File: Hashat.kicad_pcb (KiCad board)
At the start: 2 copper layers, 65 x 56.5 mm, 5 parts, among them J1 Raspberry_Pi_2_3

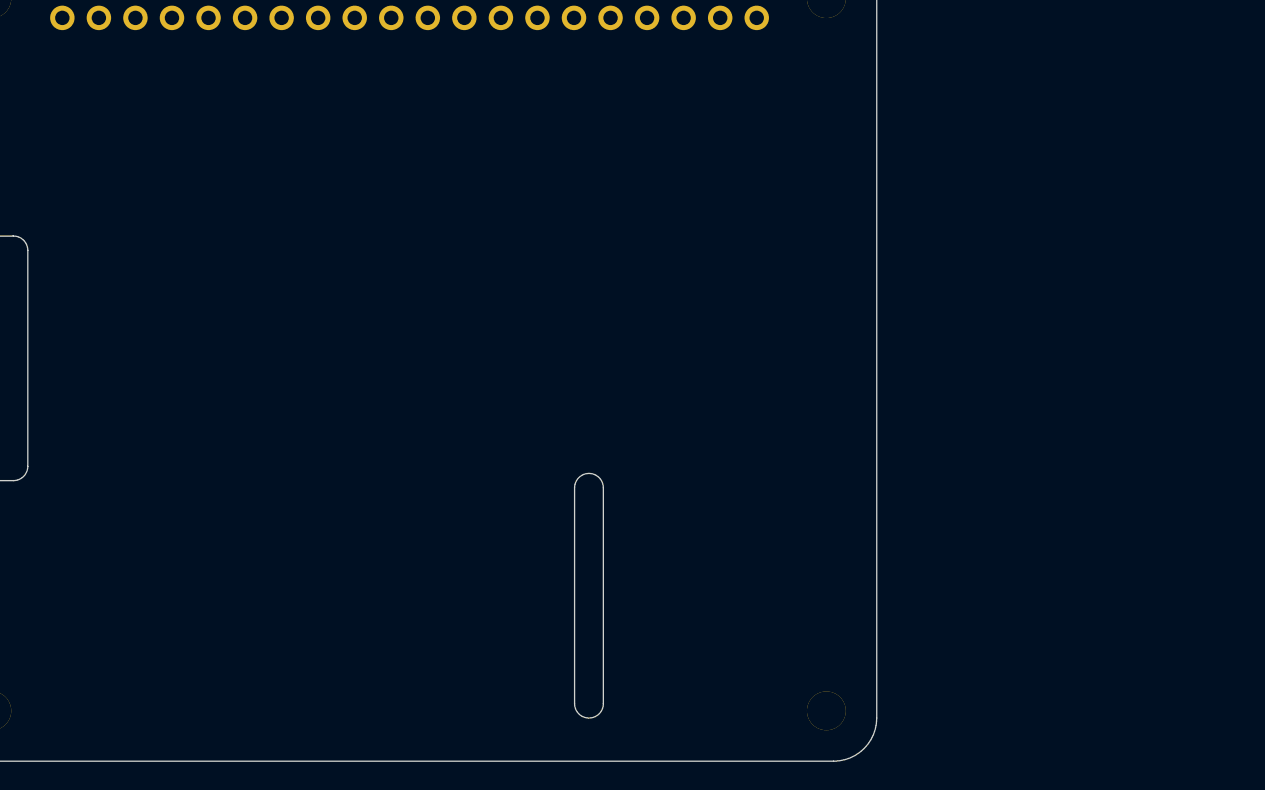
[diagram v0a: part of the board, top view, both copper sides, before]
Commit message: moved over a lot of schematic from the bitaxe
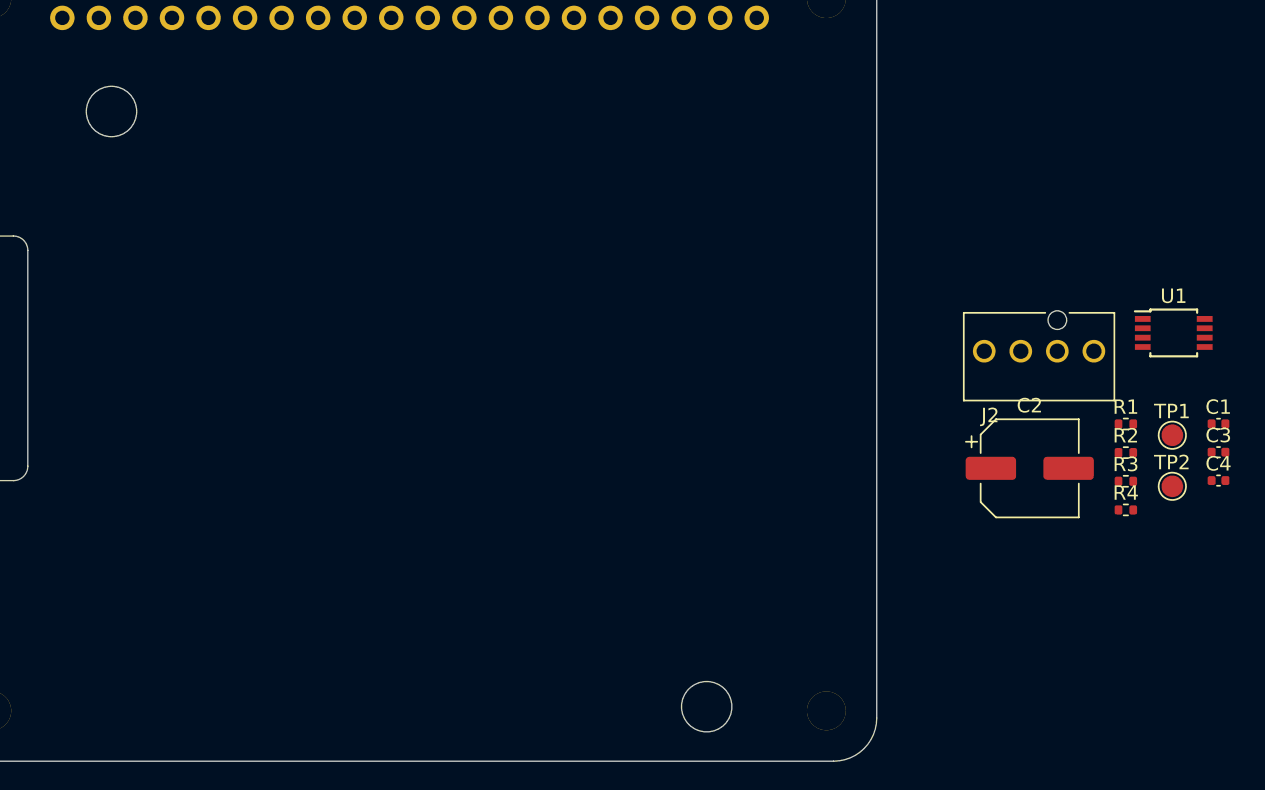
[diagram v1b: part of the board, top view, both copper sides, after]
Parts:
- added C1: 470pF, Capacitor_SMD:C_0402_1005Metric, F.Cu at (165.8, 88.6)
- added C2: 220uF, Capacitor_SMD:CP_Elec_6.3x7.7, F.Cu at (152.6, 91.6)
- added C3: 311-3342-1-ND, Capacitor_SMD:C_0402_1005Metric, F.Cu at (165.8, 90.5)
- added C4: 311-3342-1-ND, Capacitor_SMD:C_0402_1005Metric, F.Cu at (165.8, 92.5)
- added H5: MountingHole, MountingHole:MountingHole_3.5mm, F.Cu at (130.1, 108.2)
- added H6: MountingHole, MountingHole:MountingHole_3.5mm, F.Cu at (88.8, 66.8)
- added J2: Conn_01x04, bitaxe:470531000, F.Cu at (149.5, 83.5)
- added R1: 100, Resistor_SMD:R_0402_1005Metric, F.Cu at (159.3, 88.6)
- added R2: 100, Resistor_SMD:R_0402_1005Metric, F.Cu at (159.3, 90.6)
- added R3: 10k, Resistor_SMD:R_0402_1005Metric, F.Cu at (159.3, 92.5)
- added R4: 10k, Resistor_SMD:R_0402_1005Metric, F.Cu at (159.3, 94.5)
- added TP1: TestPoint, TestPoint:TestPoint_Pad_D1.5mm, F.Cu at (162.5, 89.3)
- added TP2: TestPoint, TestPoint:TestPoint_Pad_D1.5mm, F.Cu at (162.5, 92.9)
- added U1: EMC2101, Package_SO:TSSOP-8_3x3mm_P0.65mm, F.Cu at (162.6, 82.2)
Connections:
- J1 pad 1: Net-(J1-Pad1) -> unconnected-(J1-3V3-Pad1)
- J1 pad 10: Net-(J1-Pad10) -> unconnected-(J1-GPIO15/RXD-Pad10)
- J1 pad 11: Net-(J1-Pad11) -> unconnected-(J1-GPIO17-Pad11)
- J1 pad 12: Net-(J1-Pad12) -> unconnected-(J1-GPIO18/PWM0-Pad12)
- J1 pad 13: Net-(J1-Pad13) -> unconnected-(J1-GPIO27-Pad13)
- J1 pad 14: Net-(J1-Pad14) -> unconnected-(J1-GND-Pad14)
- J1 pad 15: Net-(J1-Pad15) -> unconnected-(J1-GPIO22-Pad15)
- J1 pad 16: Net-(J1-Pad16) -> unconnected-(J1-GPIO23-Pad16)
- J1 pad 17: Net-(J1-Pad17) -> unconnected-(J1-3V3-Pad17)
- J1 pad 18: Net-(J1-Pad18) -> unconnected-(J1-GPIO24-Pad18)
- J1 pad 19: Net-(J1-Pad19) -> unconnected-(J1-MOSI0/GPIO10-Pad19)
- J1 pad 2: Net-(J1-Pad2) -> unconnected-(J1-5V-Pad2)
- J1 pad 20: Net-(J1-Pad20) -> unconnected-(J1-GND-Pad20)
- J1 pad 21: Net-(J1-Pad21) -> unconnected-(J1-MISO0/GPIO9-Pad21)
- J1 pad 22: Net-(J1-Pad22) -> unconnected-(J1-GPIO25-Pad22)
- J1 pad 23: Net-(J1-Pad23) -> unconnected-(J1-SCLK0/GPIO11-Pad23)
- J1 pad 24: Net-(J1-Pad24) -> unconnected-(J1-~{CE0}/GPIO8-Pad24)
- J1 pad 25: Net-(J1-Pad25) -> unconnected-(J1-GND-Pad25)
- J1 pad 26: Net-(J1-Pad26) -> unconnected-(J1-~{CE1}/GPIO7-Pad26)
- J1 pad 27: Net-(J1-Pad27) -> unconnected-(J1-ID_SD/GPIO0-Pad27)
- J1 pad 28: Net-(J1-Pad28) -> unconnected-(J1-ID_SC/GPIO1-Pad28)
- J1 pad 29: Net-(J1-Pad29) -> unconnected-(J1-GCLK1/GPIO5-Pad29)
- J1 pad 3: Net-(J1-Pad3) -> unconnected-(J1-SDA/GPIO2-Pad3)
- J1 pad 30: Net-(J1-Pad30) -> unconnected-(J1-GND-Pad30)
- J1 pad 31: Net-(J1-Pad31) -> unconnected-(J1-GCLK2/GPIO6-Pad31)
- J1 pad 32: Net-(J1-Pad32) -> unconnected-(J1-PWM0/GPIO12-Pad32)
- J1 pad 33: Net-(J1-Pad33) -> unconnected-(J1-PWM1/GPIO13-Pad33)
- J1 pad 34: Net-(J1-Pad34) -> unconnected-(J1-GND-Pad34)
- J1 pad 35: Net-(J1-Pad35) -> unconnected-(J1-GPIO19/MISO1-Pad35)
- J1 pad 36: Net-(J1-Pad36) -> unconnected-(J1-GPIO16-Pad36)
- J1 pad 37: Net-(J1-Pad37) -> unconnected-(J1-GPIO26-Pad37)
- J1 pad 38: Net-(J1-Pad38) -> unconnected-(J1-GPIO20/MOSI1-Pad38)
- J1 pad 39: Net-(J1-Pad39) -> unconnected-(J1-GND-Pad39)
- J1 pad 4: Net-(J1-Pad4) -> unconnected-(J1-5V-Pad4)
- J1 pad 40: Net-(J1-Pad40) -> unconnected-(J1-GPIO21/SCLK1-Pad40)
- J1 pad 5: Net-(J1-Pad5) -> unconnected-(J1-SCL/GPIO3-Pad5)
- J1 pad 6: Net-(J1-Pad6) -> unconnected-(J1-GND-Pad6)
- J1 pad 7: Net-(J1-Pad7) -> unconnected-(J1-GCLK0/GPIO4-Pad7)
- J1 pad 8: Net-(J1-Pad8) -> unconnected-(J1-GPIO14/TXD-Pad8)
- J1 pad 9: Net-(J1-Pad9) -> unconnected-(J1-GND-Pad9)
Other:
- outline, holes or cut-outs redrawn

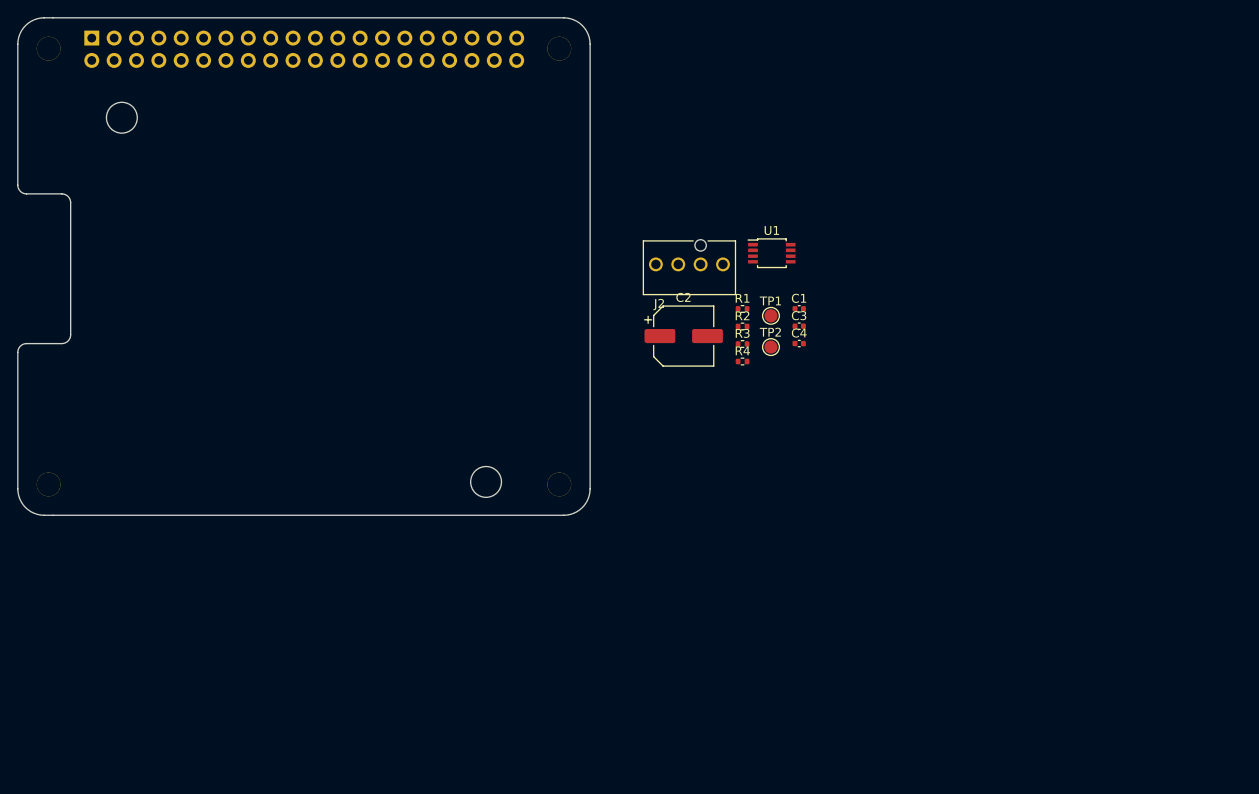
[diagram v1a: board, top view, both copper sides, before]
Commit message: more schematic. added the barrel power connector
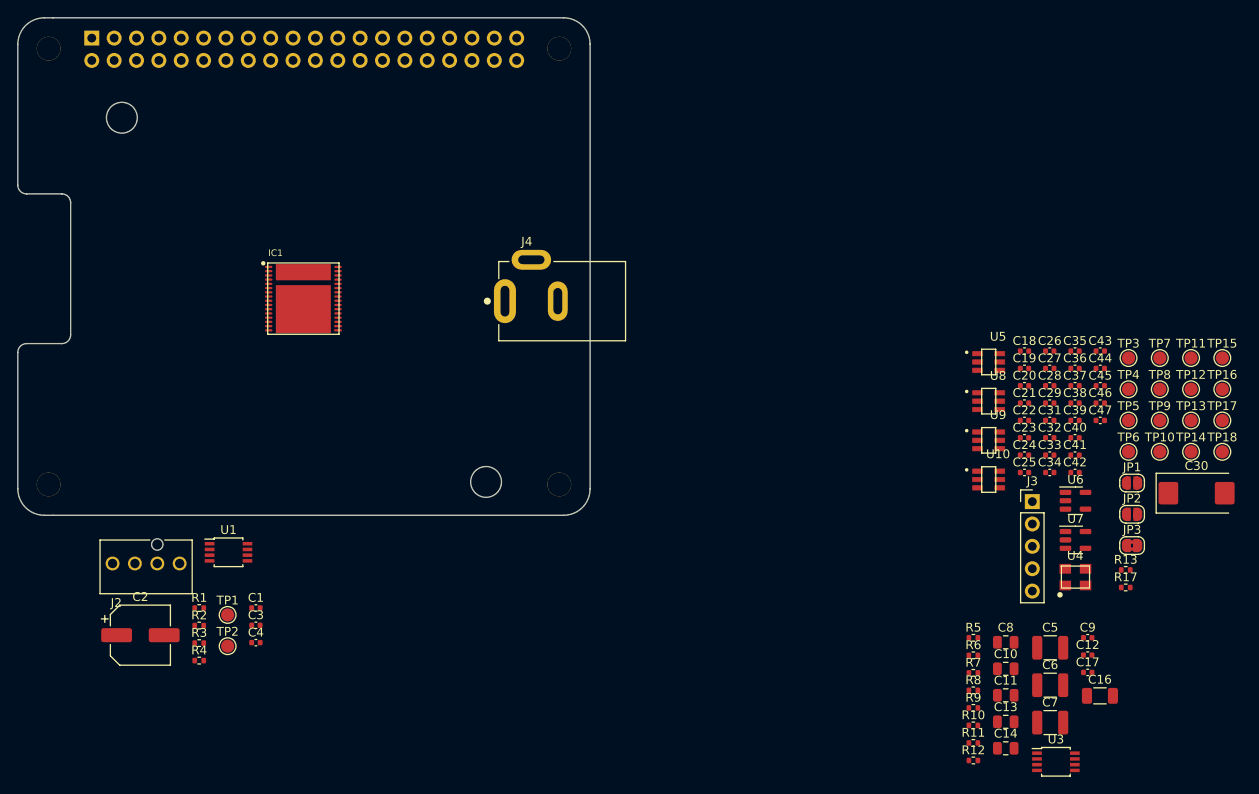
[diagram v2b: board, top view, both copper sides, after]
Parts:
- added C10: 180pF, Capacitor_SMD:C_0805_2012Metric, F.Cu at (189.2, 129.4)
- added C11: 1.5nF, Capacitor_SMD:C_0805_2012Metric, F.Cu at (189.2, 132.4)
- added C12: 0.1uF, Capacitor_SMD:C_0402_1005Metric, F.Cu at (198.5, 127.9)
- added C13: 10uF, Capacitor_SMD:C_0805_2012Metric, F.Cu at (189.2, 135.5)
- added C14: 470pF, Capacitor_SMD:C_0805_2012Metric, F.Cu at (189.2, 138.5)
- added C16: 100uF, Capacitor_SMD:C_1206_3216Metric, F.Cu at (199.9, 132.5)
- added C17: 1uF, Capacitor_SMD:C_0402_1005Metric, F.Cu at (198.5, 129.8)
- added C18: 311-3342-1-ND, Capacitor_SMD:C_0402_1005Metric, F.Cu at (191.3, 93.3)
- added C19: 587-5514-1-ND, Capacitor_SMD:C_0402_1005Metric, F.Cu at (191.3, 95.3)
- added C20: 587-5514-1-ND, Capacitor_SMD:C_0402_1005Metric, F.Cu at (191.3, 97.3)
- added C21: 587-5514-1-ND, Capacitor_SMD:C_0402_1005Metric, F.Cu at (191.3, 99.3)
- added C22: 587-5514-1-ND, Capacitor_SMD:C_0402_1005Metric, F.Cu at (191.3, 101.2)
- added C23: 587-5514-1-ND, Capacitor_SMD:C_0402_1005Metric, F.Cu at (191.3, 103.2)
- added C24: 311-3342-1-ND, Capacitor_SMD:C_0402_1005Metric, F.Cu at (191.3, 105.2)
- added C25: 587-5514-1-ND, Capacitor_SMD:C_0402_1005Metric, F.Cu at (191.3, 107.1)
- added C26: 311-3342-1-ND, Capacitor_SMD:C_0402_1005Metric, F.Cu at (194.2, 93.3)
- added C27: 587-5514-1-ND, Capacitor_SMD:C_0402_1005Metric, F.Cu at (194.2, 95.3)
- added C28: 587-5514-1-ND, Capacitor_SMD:C_0402_1005Metric, F.Cu at (194.2, 97.3)
- added C29: 587-5514-1-ND, Capacitor_SMD:C_0402_1005Metric, F.Cu at (194.2, 99.3)
- added C30: 330uF, Capacitor_Tantalum_SMD:CP_EIA-7343-31_Kemet-D_Pad2.25x2.55mm_HandSolder, F.Cu at (210.9, 109.5)
- added C31: 587-5514-1-ND, Capacitor_SMD:C_0402_1005Metric, F.Cu at (194.2, 101.2)
- added C32: 587-5514-1-ND, Capacitor_SMD:C_0402_1005Metric, F.Cu at (194.2, 103.2)
- added C33: 587-5514-1-ND, Capacitor_SMD:C_0402_1005Metric, F.Cu at (194.2, 105.2)
- added C34: 587-5514-1-ND, Capacitor_SMD:C_0402_1005Metric, F.Cu at (194.2, 107.1)
- added C35: 587-5514-1-ND, Capacitor_SMD:C_0402_1005Metric, F.Cu at (197.1, 93.3)
- added C36: 311-3342-1-ND, Capacitor_SMD:C_0402_1005Metric, F.Cu at (197.1, 95.3)
- added C37: 311-3342-1-ND, Capacitor_SMD:C_0402_1005Metric, F.Cu at (197.1, 97.3)
- added C38: 311-3342-1-ND, Capacitor_SMD:C_0402_1005Metric, F.Cu at (197.1, 99.3)
- added C39: 311-3342-1-ND, Capacitor_SMD:C_0402_1005Metric, F.Cu at (197.1, 101.2)
- added C40: 1uF, Capacitor_SMD:C_0402_1005Metric, F.Cu at (197.1, 103.2)
- added C41: 1uF, Capacitor_SMD:C_0402_1005Metric, F.Cu at (197.1, 105.2)
- added C42: 311-3342-1-ND, Capacitor_SMD:C_0402_1005Metric, F.Cu at (197.1, 107.1)
- added C43: 311-3342-1-ND, Capacitor_SMD:C_0402_1005Metric, F.Cu at (199.9, 93.3)
- added C44: 311-3342-1-ND, Capacitor_SMD:C_0402_1005Metric, F.Cu at (199.9, 95.3)
- added C45: 311-3342-1-ND, Capacitor_SMD:C_0402_1005Metric, F.Cu at (199.9, 97.3)
- added C46: 311-3342-1-ND, Capacitor_SMD:C_0402_1005Metric, F.Cu at (199.9, 99.3)
- added C47: 311-3342-1-ND, Capacitor_SMD:C_0402_1005Metric, F.Cu at (199.9, 101.2)
- added C5: 47uF, Capacitor_SMD:C_1210_3225Metric, F.Cu at (194.3, 127.0)
- added C6: 47uF, Capacitor_SMD:C_1210_3225Metric, F.Cu at (194.3, 131.3)
- added C7: 47uF, Capacitor_SMD:C_1210_3225Metric, F.Cu at (194.3, 135.5)
- added C8: 1uF, Capacitor_SMD:C_0805_2012Metric, F.Cu at (189.2, 126.4)
- added C9: 3.3nF, Capacitor_SMD:C_0402_1005Metric, F.Cu at (198.5, 125.9)
- added IC1: BM1397_mode1, bitaxe:BM1397, F.Cu at (109.4, 87.4)
- added J3: Conn_01x05, Connector_PinHeader_2.54mm:PinHeader_1x05_P2.54mm_Vertical, F.Cu at (192.2, 110.4)
- added J4: PJ-202AH, bitaxe:CUI_PJ-202AH, F.Cu at (138.8, 87.7)
- added JP1: SolderJumper_2_Open, Jumper:SolderJumper-2_P1.3mm_Open_RoundedPad1.0x1.5mm, F.Cu at (203.6, 108.3)
- added JP2: SolderJumper_2_Open, Jumper:SolderJumper-2_P1.3mm_Open_RoundedPad1.0x1.5mm, F.Cu at (203.6, 111.9)
- added JP3: SolderJumper_2_Bridged, Jumper:SolderJumper-2_P1.3mm_Bridged2Bar_RoundedPad1.0x1.5mm, F.Cu at (203.6, 115.4)
- added R10: 3.32k, Resistor_SMD:R_0402_1005Metric, F.Cu at (185.5, 135.9)
- added R11: 80k, Resistor_SMD:R_0402_1005Metric, F.Cu at (185.5, 137.9)
- added R12: DNP, Resistor_SMD:R_0402_1005Metric, F.Cu at (185.5, 139.8)
- added R13: 1k, Resistor_SMD:R_0402_1005Metric, F.Cu at (202.8, 118.2)
- added R17: 10k, Resistor_SMD:R_0402_1005Metric, F.Cu at (202.8, 120.2)
- added R5: 3.83k, Resistor_SMD:R_0402_1005Metric, F.Cu at (185.5, 125.9)
- added R6: 100k, Resistor_SMD:R_0402_1005Metric, F.Cu at (185.5, 127.9)
- added R7: 4.12k, Resistor_SMD:R_0402_1005Metric, F.Cu at (185.5, 129.9)
- added R8: 1.33k, Resistor_SMD:R_0402_1005Metric, F.Cu at (185.5, 131.9)
- added R9: 4.99k, Resistor_SMD:R_0402_1005Metric, F.Cu at (185.5, 133.9)
- added TP10: TestPoint, TestPoint:TestPoint_Pad_D1.5mm, F.Cu at (206.7, 104.8)
- added TP11: TestPoint, TestPoint:TestPoint_Pad_D1.5mm, F.Cu at (210.3, 94.1)
- added TP12: TestPoint, TestPoint:TestPoint_Pad_D1.5mm, F.Cu at (210.3, 97.7)
- added TP13: TestPoint, TestPoint:TestPoint_Pad_D1.5mm, F.Cu at (210.3, 101.2)
- added TP14: TestPoint, TestPoint:TestPoint_Pad_D1.5mm, F.Cu at (210.3, 104.8)
- added TP15: TestPoint, TestPoint:TestPoint_Pad_D1.5mm, F.Cu at (213.8, 94.1)
- added TP16: TestPoint, TestPoint:TestPoint_Pad_D1.5mm, F.Cu at (213.8, 97.7)
- added TP17: TestPoint, TestPoint:TestPoint_Pad_D1.5mm, F.Cu at (213.8, 101.2)
- added TP18: TestPoint, TestPoint:TestPoint_Pad_D1.5mm, F.Cu at (213.8, 104.8)
- added TP3: TestPoint, TestPoint:TestPoint_Pad_D1.5mm, F.Cu at (203.2, 94.1)
- added TP4: TestPoint, TestPoint:TestPoint_Pad_D1.5mm, F.Cu at (203.2, 97.7)
- added TP5: TestPoint, TestPoint:TestPoint_Pad_D1.5mm, F.Cu at (203.2, 101.2)
- added TP6: TestPoint, TestPoint:TestPoint_Pad_D1.5mm, F.Cu at (203.2, 104.8)
- added TP7: TestPoint, TestPoint:TestPoint_Pad_D1.5mm, F.Cu at (206.7, 94.1)
- added TP8: TestPoint, TestPoint:TestPoint_Pad_D1.5mm, F.Cu at (206.7, 97.7)
- added TP9: TestPoint, TestPoint:TestPoint_Pad_D1.5mm, F.Cu at (206.7, 101.2)
- added U10: SN74AXC1T45DBVR, bitaxe:SN74AXC1T45, F.Cu at (187.3, 107.9)
- added U3: DS4432U+, Package_SO:TSSOP-8_3x3mm_P0.65mm, F.Cu at (194.9, 140.0)
- added U4: 25MHz, bitaxe:O 25,0-JO32-B-1V3-1-T1-LF, F.Cu at (197.1, 119.0)
- added U5: SN74AXC1T45DBVR, bitaxe:SN74AXC1T45, F.Cu at (187.3, 94.6)
- added U6: MCP1824T-1802E, Package_TO_SOT_SMD:SOT-23-5, F.Cu at (197.1, 110.3)
- added U7: MCP1824T-0802E, Package_TO_SOT_SMD:SOT-23-5, F.Cu at (197.1, 114.8)
- added U8: SN74AXC1T45DBVR, bitaxe:SN74AXC1T45, F.Cu at (187.3, 99.0)
- added U9: SN74AXC1T45DBVR, bitaxe:SN74AXC1T45, F.Cu at (187.3, 103.5)
- moved C2 70.4 mm to (90.9, 125.6)
- moved J2 70.4 mm to (87.8, 117.5)
- moved TP2 70.4 mm to (100.8, 126.9)
- moved C1 70.4 mm to (104.0, 122.5)
- moved C3 70.4 mm to (104.0, 124.5)
- moved C4 70.4 mm to (104.0, 126.5)
- moved R1 70.4 mm to (97.6, 122.5)
- moved R2 70.4 mm to (97.6, 124.5)
- moved R4 70.4 mm to (97.6, 128.5)
- moved TP1 70.4 mm to (100.8, 123.3)
- moved U1 70.4 mm to (100.9, 116.2)
- moved R3 70.4 mm to (97.6, 126.5)
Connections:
- C2 pad 1: /Fan/5V -> /5V
- C3 pad 1: /Fan/5V -> /5V
- C4 pad 1: /Fan/3V3 -> /3V3
- J1 pad 1: unconnected-(J1-3V3-Pad1) -> /3V3
- J1 pad 10: unconnected-(J1-GPIO15/RXD-Pad10) -> /BM1397/RO
- J1 pad 11: unconnected-(J1-GPIO17-Pad11) -> /BM1397/RST
- J1 pad 14: unconnected-(J1-GND-Pad14) -> GND
- J1 pad 17: unconnected-(J1-3V3-Pad17) -> /3V3
- J1 pad 2: unconnected-(J1-5V-Pad2) -> /5V
- J1 pad 20: unconnected-(J1-GND-Pad20) -> GND
- J1 pad 25: unconnected-(J1-GND-Pad25) -> GND
- J1 pad 3: unconnected-(J1-SDA/GPIO2-Pad3) -> /Fan/SDA
- J1 pad 30: unconnected-(J1-GND-Pad30) -> GND
- J1 pad 34: unconnected-(J1-GND-Pad34) -> GND
- J1 pad 36: unconnected-(J1-GPIO16-Pad36) -> /BM1397/BI
- J1 pad 39: unconnected-(J1-GND-Pad39) -> GND
- J1 pad 4: unconnected-(J1-5V-Pad4) -> /5V
- J1 pad 5: unconnected-(J1-SCL/GPIO3-Pad5) -> /Fan/SCL
- J1 pad 6: unconnected-(J1-GND-Pad6) -> GND
- J1 pad 8: unconnected-(J1-GPIO14/TXD-Pad8) -> /BM1397/CI
- J1 pad 9: unconnected-(J1-GND-Pad9) -> GND
- J2 pad 2: /Fan/5V -> /5V
- R1 pad 2: /Fan/TEMP_N -> /BM1397/TEMP_N
- R2 pad 1: /Fan/TEMP_P -> /BM1397/TEMP_P
- R3 pad 2: /Fan/3V3 -> /3V3
- R4 pad 2: /Fan/3V3 -> /3V3
- U1 pad 1: /Fan/3V3 -> /3V3
